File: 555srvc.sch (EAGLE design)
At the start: 12 parts, among them IC2 NE555D

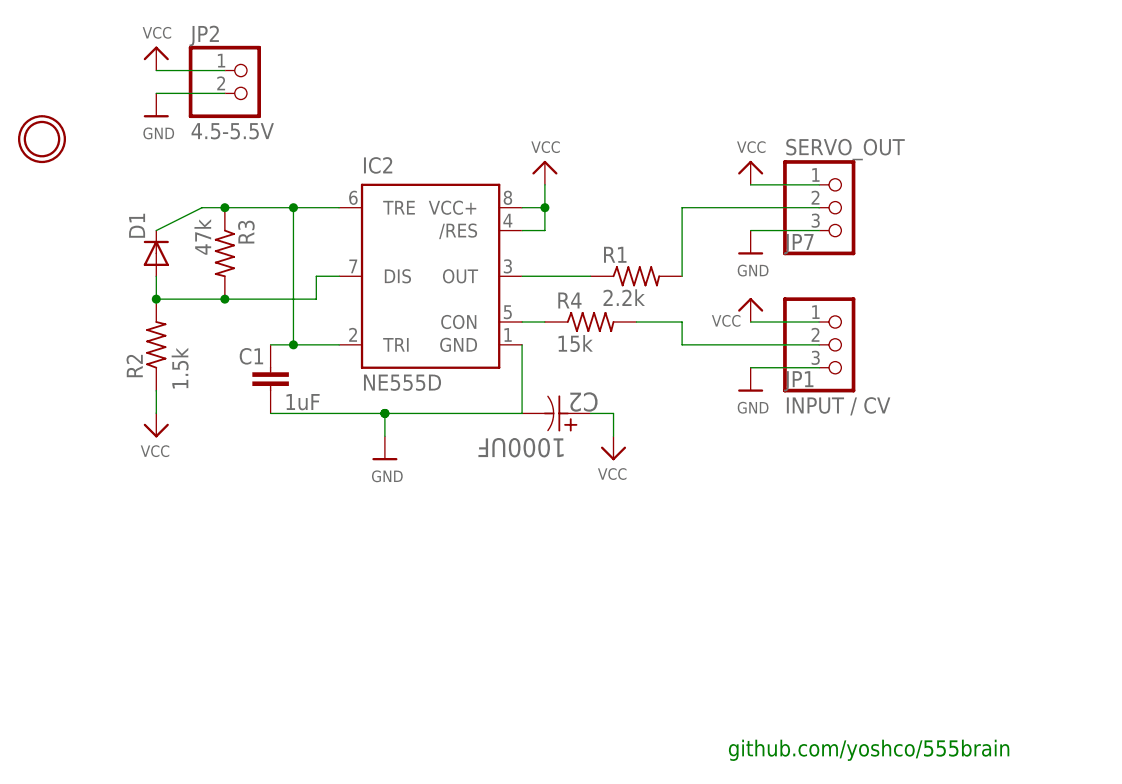
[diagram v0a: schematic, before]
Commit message: crucial wiring change for standard servo wiring on JP1 and JP2
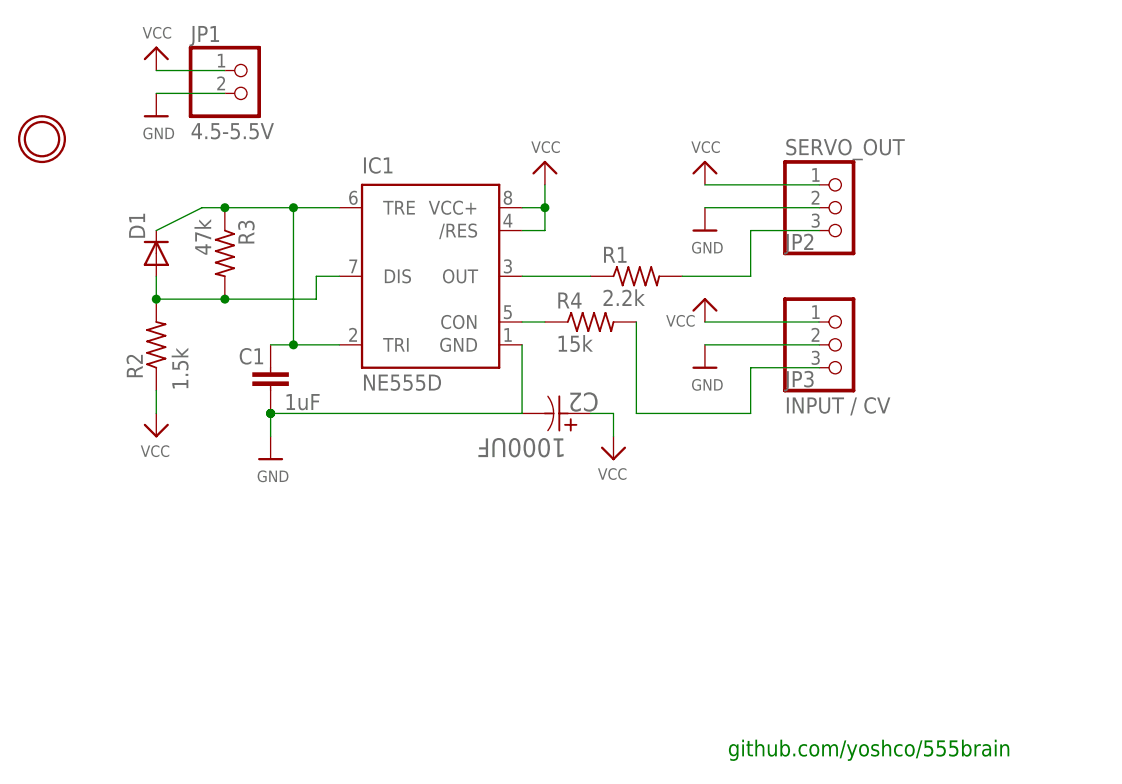
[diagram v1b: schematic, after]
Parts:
- removed JP7: SERVO_OUT, adafruit:PINHD-1X3
- added JP3: INPUT / CV, adafruit:PINHD-1X3
- JP1: value INPUT / CV -> 4.5-5.5V; device adafruit:PINHD-1X3 -> microbuilder:HEADER-1X2
- JP2: value 4.5-5.5V -> SERVO_OUT; device microbuilder:HEADER-1X2 -> adafruit:PINHD-1X3
- renumbered IC2 to IC1
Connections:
- net GND: now also JP1.2, JP3.2; no longer JP1.3, JP7.3
- net INPUT: now also JP3.3; no longer JP1.2
- net SERVO_OUT: now also JP2.3; no longer JP7.2
- net VCC: now also JP3.1; no longer JP7.1
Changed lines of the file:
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@@
 </classes>
 <parts>
-<part name="IC2" library="SparkFun-AnalogIC" deviceset="NE555" device="D" value="NE555D"/>
+<part name="IC1" library="SparkFun-AnalogIC" deviceset="NE555" device="D" value="NE555D"/>
 <part name="R1" library="adafruit" deviceset="R-US_" device="R1206" value="2.2k"/>
 <part name="R2" library="adafruit" deviceset="R-US_" device="R1206" value="1.5k"/>
@@
 <part name="P+5" library="microbuilder" deviceset="VCC" device=""/>
 <part name="U$3" library="microbuilder" deviceset="GND" device=""/>
-<part name="JP7" library="adafruit" deviceset="PINHD-1X3" device="" value="SERVO_OUT"/>
-<part name="JP1" library="adafruit" deviceset="PINHD-1X3" device="" value="INPUT / CV"/>
+<part name="JP2" library="adafruit" deviceset="PINHD-1X3" device="" value="SERVO_OUT"/>
+<part name="JP3" library="adafruit" deviceset="PINHD-1X3" device="" value="INPUT / CV"/>
 <part name="P+6" library="microbuilder" deviceset="VCC" device=""/>
 <part name="U$4" library="microbuilder" deviceset="GND" device=""/>
-<part name="JP2" library="microbuilder" deviceset="HEADER-1X2" device="" value="4.5-5.5V"/>
+<part name="JP1" library="microbuilder" deviceset="HEADER-1X2" device="" value="4.5-5.5V"/>
 <part name="FRAME1" library="frames" deviceset="A5L-LOC" device=""/>
 <part name="U$6" library="microbuilder" deviceset="MOUNTINGHOLE" device="2.0"/>
@@
 </plain>
 <instances>
-<instance part="IC2" gate="G$1" x="55.88" y="58.42"/>
+<instance part="IC1" gate="G$1" x="55.88" y="58.42"/>
 <instance part="R1" gate="G$1" x="78.74" y="58.42"/>
 <instance part="R2" gate="G$1" x="25.4" y="50.8" smashed="yes" rot="R90">
@@
 </instance>
 <instance part="P+1" gate="VCC" x="68.58" y="71.12"/>
-<instance part="U$1" gate="G$1" x="50.8" y="38.1"/>
+<instance part="U$1" gate="G$1" x="38.1" y="38.1"/>
 <instance part="C2" gate="A" x="73.66" y="43.18" smashed="yes" rot="R180">
 <attribute name="NAME" x="74.5744" y="45.4914" size="2.0828" layer="95" ratio="10" rot="SR180"/>
@@
 <instance part="P+4" gate="VCC" x="25.4" y="83.82"/>
 <instance part="U$2" gate="G$1" x="25.4" y="76.2"/>
-<instance part="P+5" gate="VCC" x="91.44" y="71.12"/>
-<instance part="U$3" gate="G$1" x="91.44" y="60.96"/>
-<instance part="JP7" gate="A" x="101.6" y="66.04" smashed="yes">
+<instance part="P+5" gate="VCC" x="86.36" y="71.12"/>
+<instance part="U$3" gate="G$1" x="86.36" y="63.5"/>
+<instance part="JP2" gate="A" x="101.6" y="66.04" smashed="yes">
 <attribute name="NAME" x="95.25" y="61.341" size="1.778" layer="95"/>
 <attribute name="VALUE" x="95.25" y="71.882" size="1.778" layer="96"/>
 </instance>
-<instance part="JP1" gate="A" x="101.6" y="50.8" smashed="yes">
+<instance part="JP3" gate="A" x="101.6" y="50.8" smashed="yes">
 <attribute name="NAME" x="95.25" y="46.101" size="1.778" layer="95"/>
 <attribute name="VALUE" x="95.25" y="43.18" size="1.778" layer="96"/>
 </instance>
-<instance part="P+6" gate="VCC" x="91.44" y="55.88" smashed="yes">
-<attribute name="VALUE" x="87.122" y="52.832" size="1.27" layer="96"/>
-</instance>
-<instance part="U$4" gate="G$1" x="91.44" y="45.72"/>
-<instance part="JP2" gate="G$1" x="35.56" y="78.74"/>
+<instance part="P+6" gate="VCC" x="86.36" y="55.88" smashed="yes">
+<attribute name="VALUE" x="82.042" y="52.832" size="1.27" layer="96"/>
+</instance>
+<instance part="U$4" gate="G$1" x="86.36" y="48.26"/>
+<instance part="JP1" gate="G$1" x="35.56" y="78.74"/>
 <instance part="FRAME1" gate="G$1" x="0" y="0"/>
 <instance part="U$6" gate="G$1" x="12.7" y="73.66"/>
@@
 <net name="VCC" class="0">
 <segment>
-<pinref part="IC2" gate="G$1" pin="VCC+"/>
+<pinref part="IC1" gate="G$1" pin="VCC+"/>
 <pinref part="P+1" gate="VCC" pin="VCC"/>
 <wire x1="66.04" y1="66.04" x2="68.58" y2="66.04" width="0.1524" layer="91"/>
 <wire x1="68.58" y1="66.04" x2="68.58" y2="68.58" width="0.1524" layer="91"/>
-<pinref part="IC2" gate="G$1" pin="/RES"/>
+<pinref part="IC1" gate="G$1" pin="/RES"/>
 <wire x1="66.04" y1="63.5" x2="68.58" y2="63.5" width="0.1524" layer="91"/>
 <wire x1="68.58" y1="63.5" x2="68.58" y2="66.04" width="0.1524" layer="91"/>
@@
 <segment>
 <pinref part="P+5" gate="VCC" pin="VCC"/>
-<wire x1="99.06" y1="68.58" x2="91.44" y2="68.58" width="0.1524" layer="91"/>
-<pinref part="JP7" gate="A" pin="1"/>
+<wire x1="99.06" y1="68.58" x2="86.36" y2="68.58" width="0.1524" layer="91"/>
+<pinref part="JP2" gate="A" pin="1"/>
 </segment>
 <segment>
 <pinref part="P+6" gate="VCC" pin="VCC"/>
-<pinref part="JP1" gate="A" pin="1"/>
-<wire x1="91.44" y1="53.34" x2="99.06" y2="53.34" width="0.1524" layer="91"/>
+<pinref part="JP3" gate="A" pin="1"/>
+<wire x1="86.36" y1="53.34" x2="99.06" y2="53.34" width="0.1524" layer="91"/>
 </segment>
 <segment>
 <pinref part="P+4" gate="VCC" pin="VCC"/>
-<pinref part="JP2" gate="G$1" pin="1"/>
+<pinref part="JP1" gate="G$1" pin="1"/>
 <wire x1="25.4" y1="81.28" x2="33.02" y2="81.28" width="0.1524" layer="91"/>
 </segment>
@@
 <pinref part="U$1" gate="G$1" pin="GND"/>
 <pinref part="C2" gate="A" pin="2"/>
-<pinref part="IC2" gate="G$1" pin="GND"/>
+<pinref part="IC1" gate="G$1" pin="GND"/>
 <wire x1="66.04" y1="50.8" x2="66.04" y2="43.18" width="0.1524" layer="91"/>
-<wire x1="50.8" y1="43.18" x2="66.04" y2="43.18" width="0.1524" layer="91"/>
-<junction x="50.8" y="43.18"/>
-<wire x1="50.8" y1="43.18" x2="50.8" y2="40.64" width="0.1524" layer="91"/>
+<wire x1="38.1" y1="43.18" x2="66.04" y2="43.18" width="0.1524" layer="91"/>
+<junction x="38.1" y="43.18"/>
+<wire x1="38.1" y1="43.18" x2="38.1" y2="40.64" width="0.1524" layer="91"/>
 <pinref part="C1" gate="G$1" pin="2"/>
-<wire x1="38.1" y1="43.18" x2="50.8" y2="43.18" width="0.1524" layer="91"/>
-<junction x="50.8" y="43.18"/>
+<junction x="38.1" y="43.18"/>
 </segment>
 <segment>
 <pinref part="U$2" gate="G$1" pin="GND"/>
-<pinref part="JP2" gate="G$1" pin="2"/>
+<pinref part="JP1" gate="G$1" pin="2"/>
 <wire x1="33.02" y1="78.74" x2="25.4" y2="78.74" width="0.1524" layer="91"/>
 </segment>
 <segment>
 <pinref part="U$3" gate="G$1" pin="GND"/>
-<wire x1="91.44" y1="63.5" x2="99.06" y2="63.5" width="0.1524" layer="91"/>
-<pinref part="JP7" gate="A" pin="3"/>
-</segment>
-<segment>
-<pinref part="JP1" gate="A" pin="3"/>
+<pinref part="JP2" gate="A" pin="2"/>
+<wire x1="86.36" y1="66.04" x2="99.06" y2="66.04" width="0.1524" layer="91"/>
+</segment>
+<segment>
 <pinref part="U$4" gate="G$1" pin="GND"/>
-<wire x1="99.06" y1="48.26" x2="91.44" y2="48.26" width="0.1524" layer="91"/>
+<pinref part="JP3" gate="A" pin="2"/>
+<wire x1="86.36" y1="50.8" x2="99.06" y2="50.8" width="0.1524" layer="91"/>
 </segment>
 </net>
 <net name="N$1" class="0">
 <segment>
-<pinref part="IC2" gate="G$1" pin="TRE"/>
+<pinref part="IC1" gate="G$1" pin="TRE"/>
 <pinref part="R3" gate="G$1" pin="1"/>
 <wire x1="45.72" y1="66.04" x2="40.64" y2="66.04" width="0.1524" layer="91"/>
@@
 <junction x="33.02" y="66.04"/>
 <pinref part="C1" gate="G$1" pin="1"/>
-<pinref part="IC2" gate="G$1" pin="TRI"/>
+<pinref part="IC1" gate="G$1" pin="TRI"/>
 <wire x1="45.72" y1="50.8" x2="40.64" y2="50.8" width="0.1524" layer="91"/>
 <wire x1="40.64" y1="50.8" x2="38.1" y2="50.8" width="0.1524" layer="91"/>
@@
 <wire x1="43.18" y1="55.88" x2="43.18" y2="58.42" width="0.1524" layer="91"/>
 <junction x="33.02" y="55.88"/>
-<pinref part="IC2" gate="G$1" pin="DIS"/>
+<pinref part="IC1" gate="G$1" pin="DIS"/>
 <wire x1="43.18" y1="58.42" x2="45.72" y2="58.42" width="0.1524" layer="91"/>
 </segment>
@@
 <net name="N$4" class="0">
 <segment>
-<pinref part="IC2" gate="G$1" pin="CON"/>
+<pinref part="IC1" gate="G$1" pin="CON"/>
 <pinref part="R4" gate="G$1" pin="1"/>
 <wire x1="66.04" y1="53.34" x2="68.58" y2="53.34" width="0.1524" layer="91"/>
@@
 <net name="N$5" class="0">
 <segment>
-<pinref part="IC2" gate="G$1" pin="OUT"/>
+<pinref part="IC1" gate="G$1" pin="OUT"/>
 <pinref part="R1" gate="G$1" pin="1"/>
 <wire x1="66.04" y1="58.42" x2="73.66" y2="58.42" width="0.1524" layer="91"/>
@@
 <segment>
 <pinref part="R1" gate="G$1" pin="2"/>
-<wire x1="83.82" y1="58.42" x2="83.82" y2="66.04" width="0.1524" layer="91"/>
-<wire x1="83.82" y1="66.04" x2="99.06" y2="66.04" width="0.1524" layer="91"/>
-<pinref part="JP7" gate="A" pin="2"/>
+<pinref part="JP2" gate="A" pin="3"/>
+<wire x1="99.06" y1="63.5" x2="91.44" y2="63.5" width="0.1524" layer="91"/>
+<wire x1="91.44" y1="63.5" x2="91.44" y2="58.42" width="0.1524" layer="91"/>
+<wire x1="91.44" y1="58.42" x2="83.82" y2="58.42" width="0.1524" layer="91"/>
 </segment>
 </net>
@@
 <segment>
 <pinref part="R4" gate="G$1" pin="2"/>
-<wire x1="99.06" y1="50.8" x2="83.82" y2="50.8" width="0.1524" layer="91"/>
-<wire x1="83.82" y1="50.8" x2="83.82" y2="53.34" width="0.1524" layer="91"/>
-<wire x1="83.82" y1="53.34" x2="78.74" y2="53.34" width="0.1524" layer="91"/>
-<pinref part="JP1" gate="A" pin="2"/>
-</segment>
-</net>
+<pinref part="JP3" gate="A" pin="3"/>
+<wire x1="99.06" y1="48.26" x2="91.44" y2="48.26" width="0.1524" layer="91"/>
+<wire x1="91.44" y1="48.26" x2="91.44" y2="43.18" width="0.1524" layer="91"/>
+<wire x1="91.44" y1="43.18" x2="78.74" y2="43.18" width="0.1524" layer="91"/>
+<wire x1="78.74" y1="43.18" x2="78.74" y2="53.34" width="0.1524" layer="91"/>
+</segment>
+</net>

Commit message: smd added schema and board pdf,png
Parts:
- IC1: value NE555D -> 555
- JP1: device microbuilder:HEADER-1X2 -> microbuilder:HEADER-1X2ROUND
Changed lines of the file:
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@@
 </classes>
 <parts>
-<part name="IC1" library="SparkFun-AnalogIC" deviceset="NE555" device="D" value="NE555D"/>
+<part name="IC1" library="SparkFun-AnalogIC" deviceset="NE555" device="D" value="555"/>
 <part name="R1" library="adafruit" deviceset="R-US_" device="R1206" value="2.2k"/>
 <part name="R2" library="adafruit" deviceset="R-US_" device="R1206" value="1.5k"/>
@@
 <part name="P+6" library="microbuilder" deviceset="VCC" device=""/>
 <part name="U$4" library="microbuilder" deviceset="GND" device=""/>
-<part name="JP1" library="microbuilder" deviceset="HEADER-1X2" device="" value="4.5-5.5V"/>
+<part name="JP1" library="microbuilder" deviceset="HEADER-1X2" device="ROUND" value="4.5-5.5V"/>
 <part name="FRAME1" library="frames" deviceset="A5L-LOC" device=""/>
 <part name="U$6" library="microbuilder" deviceset="MOUNTINGHOLE" device="2.0"/>

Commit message: smd wip
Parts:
- removed JP1: 4.5-5.5V, microbuilder:HEADER-1X2ROUND
- removed U$6: MOUNTINGHOLE2.0, microbuilder:MOUNTINGHOLE2.0
- C1: device SparkFun-Capacitors:CAP1206 -> ATtami:RESISTOR0805-RES
- C2: device Panasonic-EEE0_EEE1_EEE2_EEEFC:EEE-FC0J102AP-CASE-G -> Panasonic-EEE0_EEE1_EEE2_EEEFC:EEE-1AA102P-CASE-G
- R1, R2, R3, R4: device adafruit:R-US_R1206 -> ATtami:RESISTOR0805-RES
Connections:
- net GND: no longer JP1.2
- net VCC: no longer JP1.1
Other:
- moved on the sheet: C2
